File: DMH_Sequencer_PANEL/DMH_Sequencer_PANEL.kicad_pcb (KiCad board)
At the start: 2 copper layers, 100 x 200 mm, 5 parts, among them J0 Panel_GND_Solder_Wire_Pad

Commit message: Main controls position test ongoing
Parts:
- added H1: LED Step 1, SynthStuff:MountingHole_LED_3mm_R, F.Cu at (124.0, 46.5)
- added H10: CV 2, SynthStuff:Pot_Cutout_Small, F.Cu at (154.0, 65.0)
- added H1003: MountingHole_Rails, SynthStuff:MountingHole_Rails, F.Cu at (250.0, 33.5)
- added H1004: MountingHole_Rails, SynthStuff:MountingHole_Rails, F.Cu at (346.5, 33.5)
- added H1007: MountingHole_Rails, SynthStuff:MountingHole_Rails, F.Cu at (250.0, 226.5)
- added H1008: MountingHole_Rails, SynthStuff:MountingHole_Rails, F.Cu at (346.5, 226.5)
- added H11: CV 3, SynthStuff:Pot_Cutout_Small, F.Cu at (184.0, 65.0)
- added H12: CV 4, SynthStuff:Pot_Cutout_Small, F.Cu at (214.0, 65.0)
- added H13: CV 5, SynthStuff:Pot_Cutout_Small, F.Cu at (244.0, 65.0)
- added H14: CV 6, SynthStuff:Pot_Cutout_Small, F.Cu at (274.0, 65.0)
- added H15: CV 7, SynthStuff:Pot_Cutout_Small, F.Cu at (304.0, 65.0)
- added H16: CV 8, SynthStuff:Pot_Cutout_Small, F.Cu at (334.0, 65.0)
- added H17: GL 1, SynthStuff:Pot_Cutout_Tiny_gate_P110KH1, F.Cu at (124.0, 94.5)
- added H18: GL 2, SynthStuff:Pot_Cutout_Tiny_gate_P110KH1, F.Cu at (154.0, 94.5)
- added H19: GL 3, SynthStuff:Pot_Cutout_Tiny_gate_P110KH1, F.Cu at (184.0, 94.5)
- added H2: LED Step 2, SynthStuff:MountingHole_LED_3mm_R, F.Cu at (154.0, 46.5)
- added H20: GL 4, SynthStuff:Pot_Cutout_Tiny_gate_P110KH1, F.Cu at (214.0, 94.5)
- added H21: GL 5, SynthStuff:Pot_Cutout_Tiny_gate_P110KH1, F.Cu at (244.0, 94.5)
- added H22: GL 6, SynthStuff:Pot_Cutout_Tiny_gate_P110KH1, F.Cu at (274.0, 94.5)
- added H23: GL 7, SynthStuff:Pot_Cutout_Tiny_gate_P110KH1, F.Cu at (304.0, 94.5)
- added H24: GL 8, SynthStuff:Pot_Cutout_Tiny_gate_P110KH1, F.Cu at (334.0, 94.5)
- added H25: Slew 1, SynthStuff:Toggle_Switch_TE_Cutout, F.Cu at (598.6, 10.5)
- added H26: Slew 2, SynthStuff:Toggle_Switch_TE_Cutout, F.Cu at (613.7, 10.5)
- added H27: Slew 3, SynthStuff:Toggle_Switch_TE_Cutout, F.Cu at (628.7, 10.5)
- added H28: Slew 4, SynthStuff:Toggle_Switch_TE_Cutout, F.Cu at (643.7, 10.5)
- added H29: Slew 5, SynthStuff:Toggle_Switch_TE_Cutout, F.Cu at (598.6, 26.4)
- added H3: LED Step 3, SynthStuff:MountingHole_LED_3mm_R, F.Cu at (184.0, 46.5)
- added H30: Slew 6, SynthStuff:Toggle_Switch_TE_Cutout, F.Cu at (613.7, 26.4)
- added H31: Slew 7, SynthStuff:Toggle_Switch_TE_Cutout, F.Cu at (628.7, 26.4)
- added H32: Slew 8, SynthStuff:Toggle_Switch_TE_Cutout, F.Cu at (643.7, 26.4)
- added H33: LED Step 9, SynthStuff:MountingHole_LED_3mm_R, F.Cu at (605.0, 68.6)
- added H34: LED Step 10, SynthStuff:MountingHole_LED_3mm_R, F.Cu at (605.0, 74.1)
- added H35: LED Step 11, SynthStuff:MountingHole_LED_3mm_R, F.Cu at (605.0, 79.7)
- added H36: LED Step 12, SynthStuff:MountingHole_LED_3mm_R, F.Cu at (605.0, 85.2)
- added H37: LED Step 13, SynthStuff:MountingHole_LED_3mm_R, F.Cu at (610.6, 68.6)
- added H38: LED Step 14, SynthStuff:MountingHole_LED_3mm_R, F.Cu at (610.6, 74.1)
- added H39: LED Step 15, SynthStuff:MountingHole_LED_3mm_R, F.Cu at (610.6, 79.7)
- added H4: LED Step 4, SynthStuff:MountingHole_LED_3mm_R, F.Cu at (214.0, 46.5)
- added H40: LED Step 16, SynthStuff:MountingHole_LED_3mm_R, F.Cu at (610.6, 85.2)
- added H41: CV 9, SynthStuff:Pot_Cutout_Small, F.Cu at (543.9, 17.8)
- added H42: CV 10, SynthStuff:Pot_Cutout_Small, F.Cu at (543.9, 47.3)
- added H43: CV 11, SynthStuff:Pot_Cutout_Small, F.Cu at (543.9, 76.8)
- added H44: CV 12, SynthStuff:Pot_Cutout_Small, F.Cu at (543.9, 106.3)
- added H45: CV 13, SynthStuff:Pot_Cutout_Small, F.Cu at (575.4, 17.8)
- added H46: CV 14, SynthStuff:Pot_Cutout_Small, F.Cu at (575.4, 47.3)
- added H47: CV 15, SynthStuff:Pot_Cutout_Small, F.Cu at (575.4, 76.8)
- added H48: CV 16, SynthStuff:Pot_Cutout_Small, F.Cu at (575.4, 106.3)
- added H49: GL 9, SynthStuff:Pot_Cutout_Tiny_gate_P110KH1, F.Cu at (528.9, 132.8)
- added H5: LED Step 5, SynthStuff:MountingHole_LED_3mm_R, F.Cu at (244.0, 46.5)
- added H50: GL 10, SynthStuff:Pot_Cutout_Tiny_gate_P110KH1, F.Cu at (528.9, 157.1)
- added H51: GL 11, SynthStuff:Pot_Cutout_Tiny_gate_P110KH1, F.Cu at (528.9, 181.3)
- added H52: GL 12, SynthStuff:Pot_Cutout_Tiny_gate_P110KH1, F.Cu at (528.9, 205.6)
- added H53: GL 13, SynthStuff:Pot_Cutout_Tiny_gate_P110KH1, F.Cu at (554.4, 132.8)
- added H54: GL 14, SynthStuff:Pot_Cutout_Tiny_gate_P110KH1, F.Cu at (554.4, 157.1)
- added H55: GL 15, SynthStuff:Pot_Cutout_Tiny_gate_P110KH1, F.Cu at (554.4, 181.3)
- added H56: GL 16, SynthStuff:Pot_Cutout_Tiny_gate_P110KH1, F.Cu at (554.4, 205.6)
- added H57: Slew 9, SynthStuff:Toggle_Switch_TE_Cutout, F.Cu at (598.6, 42.4)
- added H58: Slew 10, SynthStuff:Toggle_Switch_TE_Cutout, F.Cu at (613.7, 42.4)
- added H59: Slew 11, SynthStuff:Toggle_Switch_TE_Cutout, F.Cu at (628.7, 42.4)
- added H6: LED Step 6, SynthStuff:MountingHole_LED_3mm_R, F.Cu at (274.0, 46.5)
- added H60: Slew 12, SynthStuff:Toggle_Switch_TE_Cutout, F.Cu at (643.7, 42.4)
- added H61: Slew 13, SynthStuff:Toggle_Switch_TE_Cutout, F.Cu at (598.6, 58.3)
- added H62: Slew 14, SynthStuff:Toggle_Switch_TE_Cutout, F.Cu at (613.7, 58.3)
- added H63: Slew 15, SynthStuff:Toggle_Switch_TE_Cutout, F.Cu at (628.7, 58.3)
- added H64: Slew 16, SynthStuff:Toggle_Switch_TE_Cutout, F.Cu at (643.7, 58.3)
- added H65: Gate Out 1, SynthStuff:Jack_6.35mm_Cutout_Output_v6, F.Cu at (575.7, 128.6)
- added H66: Gate Out 2, SynthStuff:Jack_6.35mm_Cutout_Output_v6, F.Cu at (575.7, 145.7)
- added H67: Gate Out 3, SynthStuff:Jack_6.35mm_Cutout_Output_v6, F.Cu at (592.8, 128.6)
- added H68: Gate Out 4, SynthStuff:Jack_6.35mm_Cutout_Output_v6, F.Cu at (592.8, 145.7)
- added H69: Gate Out 5, SynthStuff:Jack_6.35mm_Cutout_Output_v6, F.Cu at (609.9, 128.6)
- added H7: LED Step 7, SynthStuff:MountingHole_LED_3mm_R, F.Cu at (304.0, 46.5)
- added H70: Gate Out 6, SynthStuff:Jack_6.35mm_Cutout_Output_v6, F.Cu at (609.9, 145.7)
- added H71: Gate Out 7, SynthStuff:Jack_6.35mm_Cutout_Output_v6, F.Cu at (627.0, 128.6)
- added H72: Gate Out 8, SynthStuff:Jack_6.35mm_Cutout_Output_v6, F.Cu at (627.0, 145.7)
- added H8: LED Step 8, SynthStuff:MountingHole_LED_3mm_R, F.Cu at (334.0, 46.5)
- added H9: CV 1, SynthStuff:Pot_Cutout_Small, F.Cu at (124.0, 65.0)
- moved H1002 3.50 mm to (150.0, 33.5)
- moved H1006 3.50 mm to (150.0, 226.5)
- renumbered H1 to H1001, H2 to H1002, H3 to H1005, H4 to H1006
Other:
- board size 100 x 200 mm -> 300 x 200 mm
- board text added: "Sequencer"
- board text removed: "Name"

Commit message: First Layout ready
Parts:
- removed H65: Gate Out 1, SynthStuff:Jack_6.35mm_Cutout_Output_v6
- removed H66: Gate Out 2, SynthStuff:Jack_6.35mm_Cutout_Output_v6
- removed H67: Gate Out 3, SynthStuff:Jack_6.35mm_Cutout_Output_v6
- removed H68: Gate Out 4, SynthStuff:Jack_6.35mm_Cutout_Output_v6
- removed H69: Gate Out 5, SynthStuff:Jack_6.35mm_Cutout_Output_v6
- removed H70: Gate Out 6, SynthStuff:Jack_6.35mm_Cutout_Output_v6
- removed H71: Gate Out 7, SynthStuff:Jack_6.35mm_Cutout_Output_v6
- removed H72: Gate Out 8, SynthStuff:Jack_6.35mm_Cutout_Output_v6
- added H73: Clock, SynthStuff:Pot_Cutout_Medium_v2, F.Cu at (80.5, 55.0)
- added H75: Transp, SynthStuff:Pot_Cutout_Tiny, F.Cu at (94.5, 87.0)
- added H77: Slew, SynthStuff:Pot_Cutout_Tiny, F.Cu at (66.5, 87.0)
- added H79: Direction, SynthStuff:Selector_Cutout_5pos, F.Cu at (80.5, 121.5)
- added H80: Mode, SynthStuff:Toggle_Switch_TE_Cutout, F.Cu at (95.0, 171.0)
- added H81: Clock, SynthStuff:Toggle_Switch_TE_Cutout, F.Cu at (66.0, 171.0)
- added H82: Quant, SynthStuff:Toggle_Switch_TE_Cutout, F.Cu at (80.5, 171.0)
- added H83: Step, SynthStuff:MX_switch_Cutout, F.Cu at (66.0, 148.0)
- added H84: Reset, SynthStuff:MX_switch_Cutout, F.Cu at (95.0, 148.0)
- added H85: LED Quant, SynthStuff:MountingHole_LED_3mm_R, F.Cu at (80.5, 148.0)
- added H86: CV 1-8, SynthStuff:Jack_6.35mm_Cutout_Output_v6, F.Cu at (63.4, 208.8)
- added H87: CV 9-16, SynthStuff:Jack_6.35mm_Cutout_Output_v6, F.Cu at (80.5, 208.8)
- added H88: Gate, SynthStuff:Jack_6.35mm_Cutout_Output_v6, F.Cu at (97.6, 208.8)
- added H90: Clock, SynthStuff:Jack_6.35mm_Cutout_v3, F.Cu at (63.4, 190.2)
- added H91: Reset, SynthStuff:Jack_6.35mm_Cutout_v3, F.Cu at (80.5, 190.2)
- added H92: Transp, SynthStuff:Jack_6.35mm_Cutout_v3, F.Cu at (97.6, 190.2)
- moved H57 502.9 mm to (124.0, 208.5)
- moved H58 488.8 mm to (154.0, 208.5)
- moved H25 486.7 mm to (124.0, 118.0)
- moved H33 485.6 mm to (124.0, 135.5)
- moved H59 474.7 mm to (184.0, 208.5)
- moved H26 472.1 mm to (154.0, 118.0)
- moved H60 460.7 mm to (214.0, 208.5)
- moved H27 457.5 mm to (184.0, 118.0)
- moved H34 455.2 mm to (154.0, 135.5)
- moved H28 442.9 mm to (214.0, 118.0)
- moved H41 441.4 mm to (124.0, 154.0)
- moved H35 424.7 mm to (184.0, 135.5)
- moved H49 408.2 mm to (124.0, 185.0)
- moved H42 404.2 mm to (154.0, 154.0)
- moved H36 394.2 mm to (214.0, 135.5)
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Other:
- board text added: "1x16"
- board text added: "2x8"
- board text added: "Dis"
- board text added: "En"

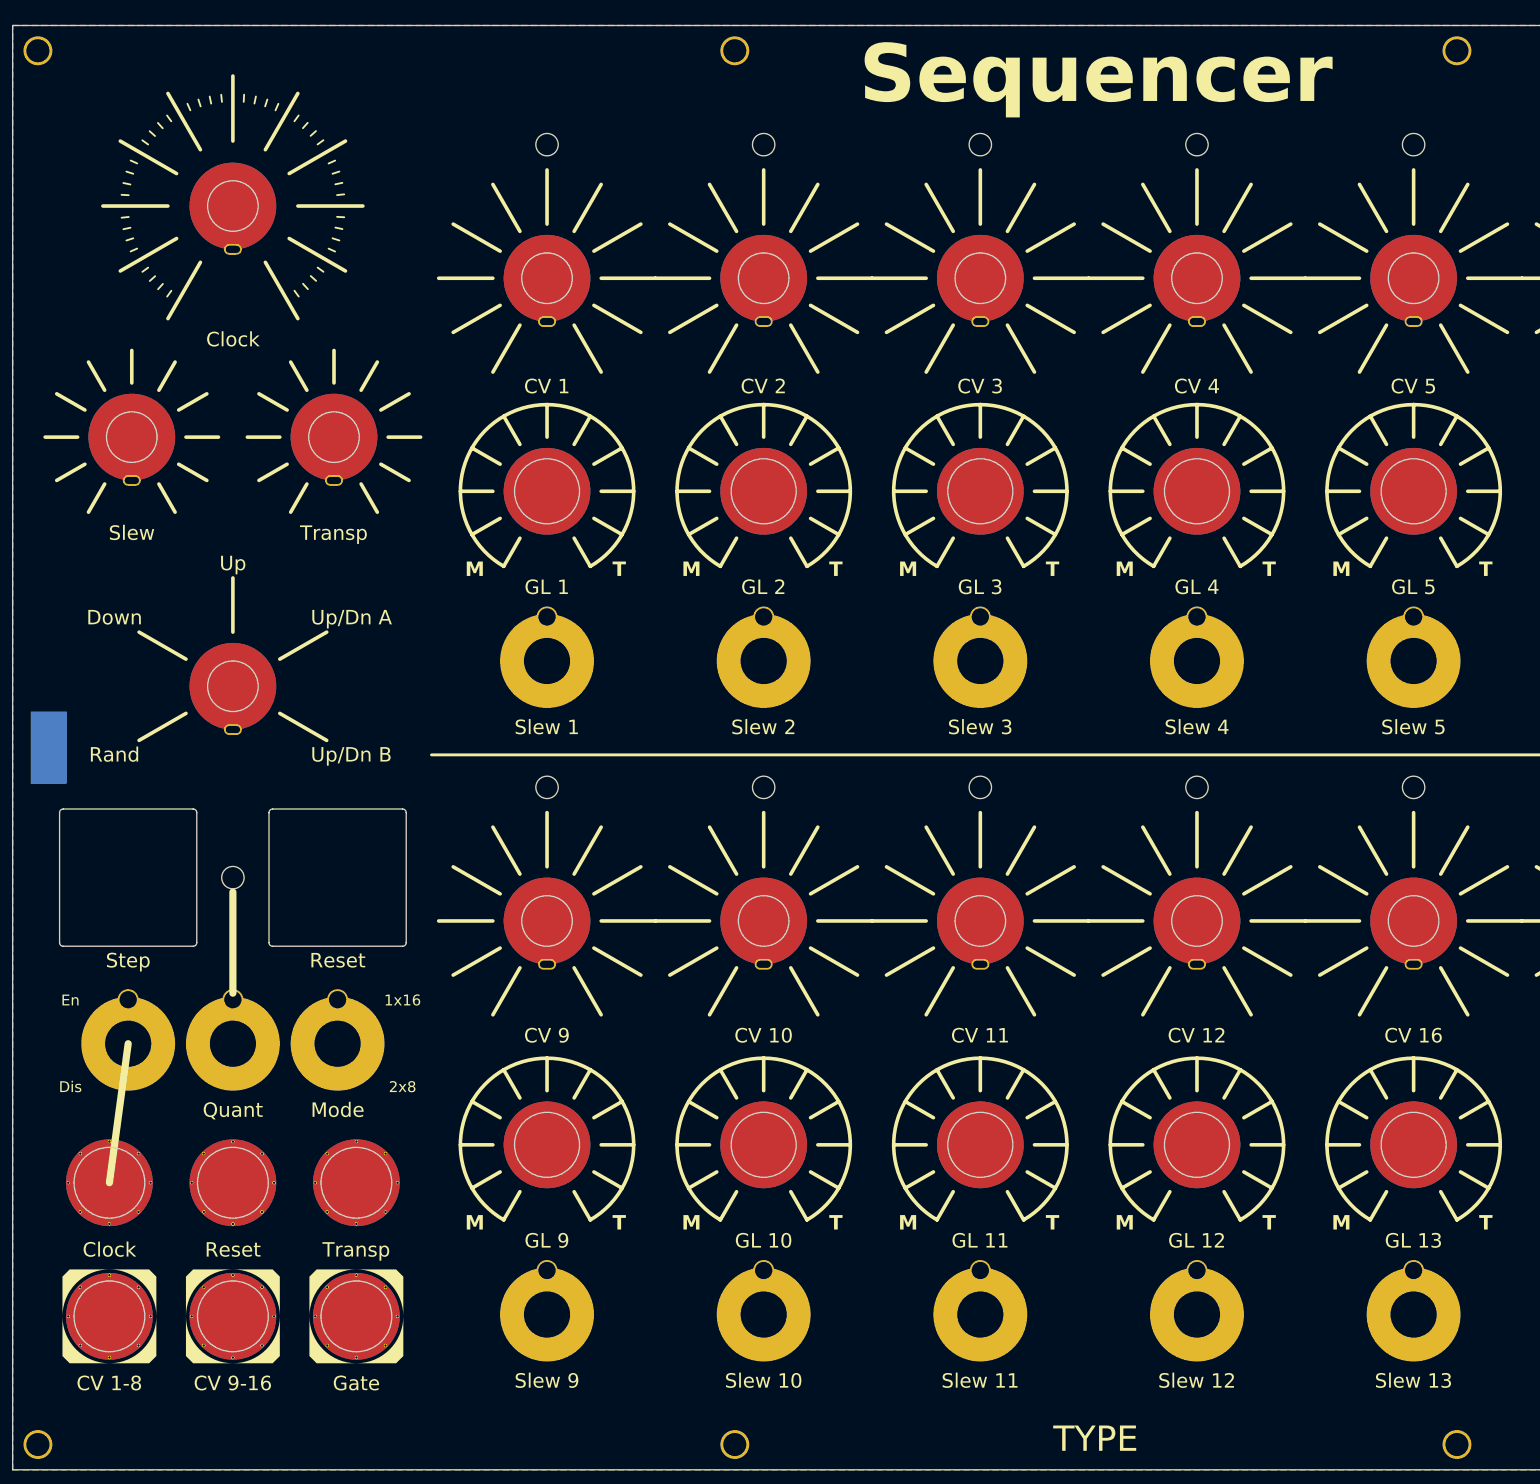
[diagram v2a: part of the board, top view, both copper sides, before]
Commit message: Updated selector 3D model
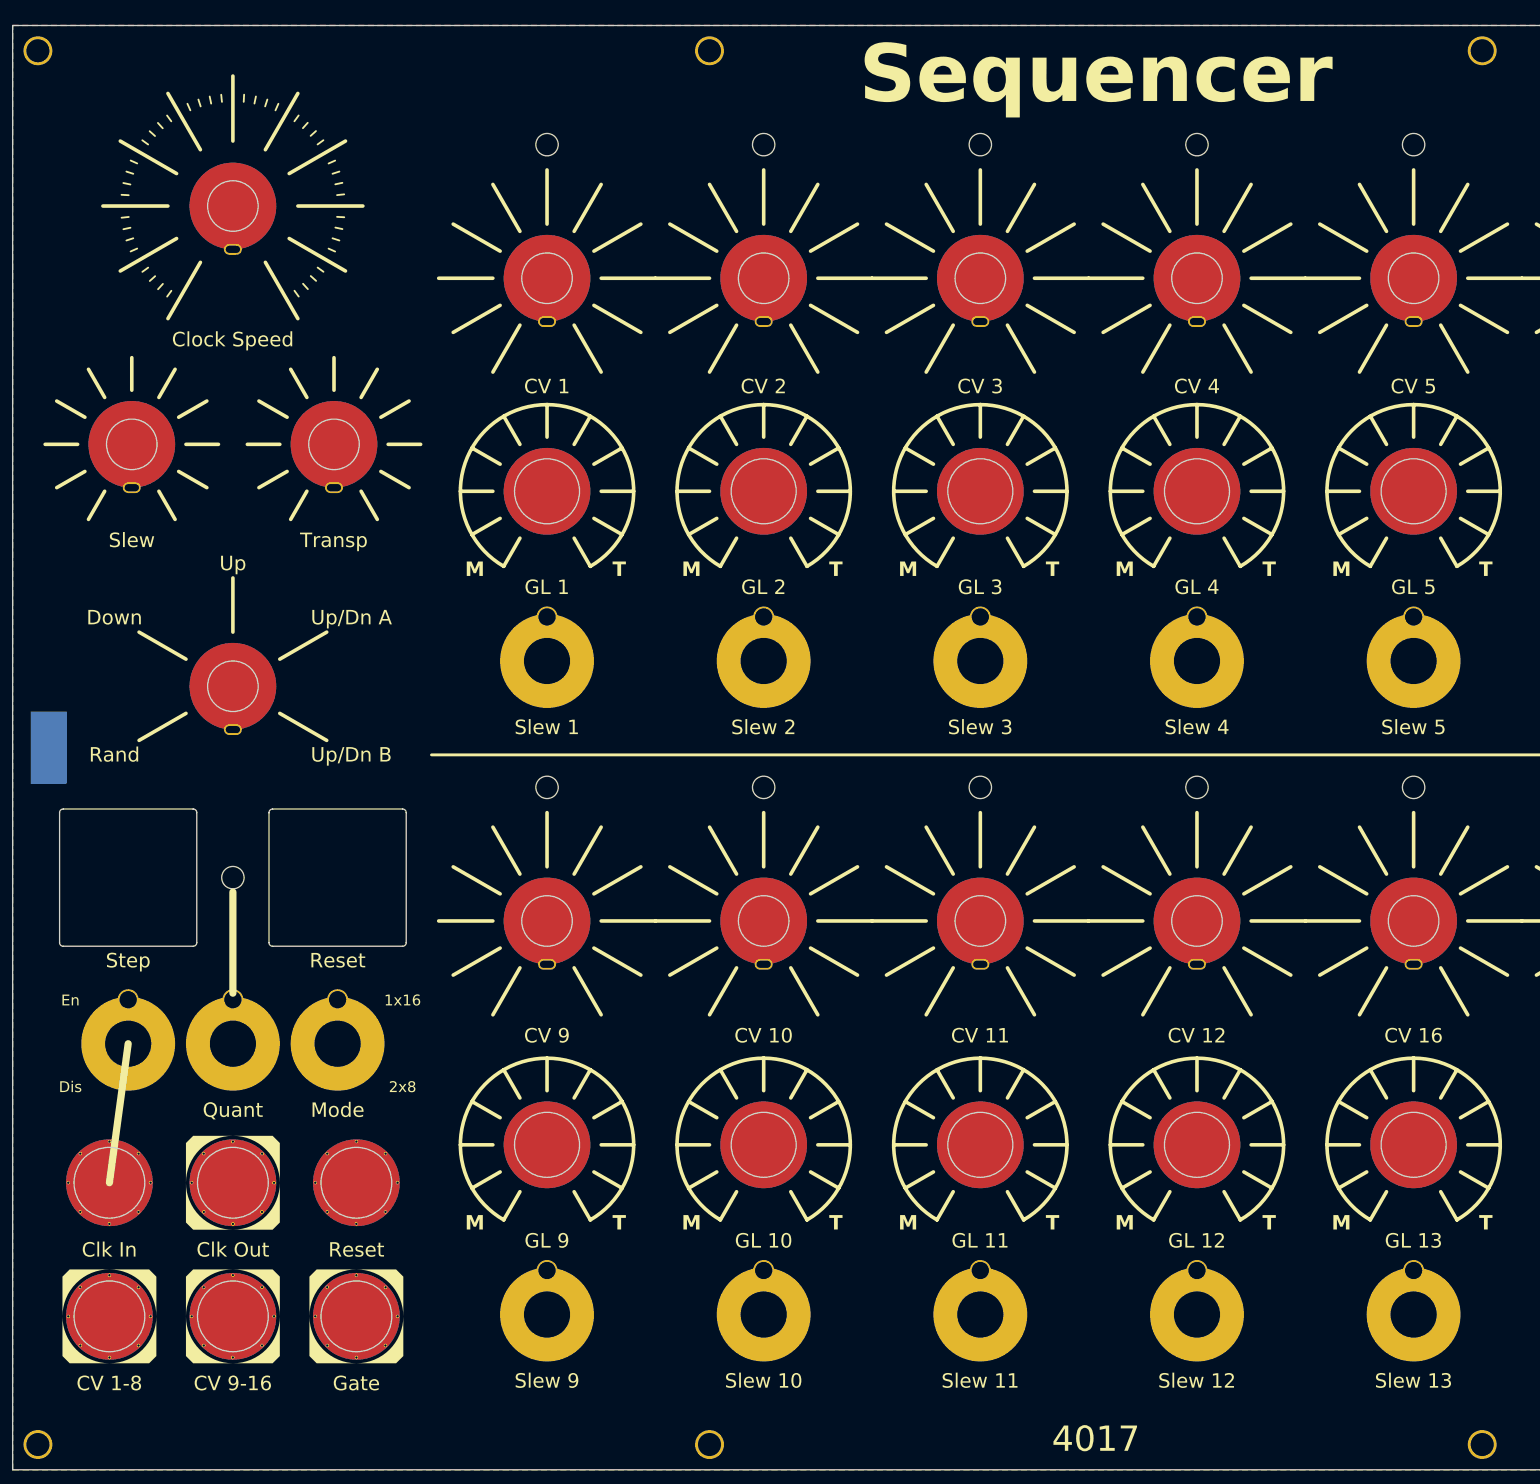
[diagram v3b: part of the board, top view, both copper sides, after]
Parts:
- removed H92: Transp, SynthStuff:Jack_6.35mm_Cutout_v3
- added H97: Clk Out, SynthStuff:Jack_6.35mm_Cutout_Output_v6, F.Cu at (80.5, 190.2)
- H73: value Clock -> Clock Speed
- H85: footprint SynthStuff:MountingHole_LED_3mm_R -> SynthStuff:MountingHole_LED_3mm_B
- H90: value Clock -> Clk In
- moved H91 17.1 mm to (97.6, 190.2)
- moved H1002 3.50 mm to (146.5, 33.5)
- moved H1003 3.50 mm to (253.5, 33.5)
- moved H1006 3.50 mm to (146.5, 226.5)
- moved H1007 3.50 mm to (253.5, 226.5)
- moved H75 1.00 mm to (94.5, 88.0)
- moved H77 1.00 mm to (66.5, 88.0)
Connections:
- H10 pad 1: unconnected-(H10-Pad1) -> GND
- H11 pad 1: unconnected-(H11-Pad1) -> GND
- H12 pad 1: unconnected-(H12-Pad1) -> GND
- H13 pad 1: unconnected-(H13-Pad1) -> GND
- H14 pad 1: unconnected-(H14-Pad1) -> GND
- H15 pad 1: unconnected-(H15-Pad1) -> GND
- H16 pad 1: unconnected-(H16-Pad1) -> GND
- H17 pad 1: unconnected-(H17-Pad1) -> GND
- H18 pad 1: unconnected-(H18-Pad1) -> GND
- H19 pad 1: unconnected-(H19-Pad1) -> GND
- H20 pad 1: unconnected-(H20-Pad1) -> GND
- H21 pad 1: unconnected-(H21-Pad1) -> GND
- H22 pad 1: unconnected-(H22-Pad1) -> GND
- H23 pad 1: unconnected-(H23-Pad1) -> GND
- H24 pad 1: unconnected-(H24-Pad1) -> GND
- H25 pad 1: unconnected-(H25-Pad1) -> GND
- H26 pad 1: unconnected-(H26-Pad1) -> GND
- H27 pad 1: unconnected-(H27-Pad1) -> GND
- H28 pad 1: unconnected-(H28-Pad1) -> GND
- H29 pad 1: unconnected-(H29-Pad1) -> GND
- H30 pad 1: unconnected-(H30-Pad1) -> GND
- H31 pad 1: unconnected-(H31-Pad1) -> GND
- H32 pad 1: unconnected-(H32-Pad1) -> GND
- H41 pad 1: unconnected-(H41-Pad1) -> GND
- H42 pad 1: unconnected-(H42-Pad1) -> GND
- H43 pad 1: unconnected-(H43-Pad1) -> GND
- H44 pad 1: unconnected-(H44-Pad1) -> GND
- H45 pad 1: unconnected-(H45-Pad1) -> GND
- H46 pad 1: unconnected-(H46-Pad1) -> GND
- H47 pad 1: unconnected-(H47-Pad1) -> GND
- H48 pad 1: unconnected-(H48-Pad1) -> GND
- H49 pad 1: unconnected-(H49-Pad1) -> GND
- H50 pad 1: unconnected-(H50-Pad1) -> GND
- H51 pad 1: unconnected-(H51-Pad1) -> GND
- H52 pad 1: unconnected-(H52-Pad1) -> GND
- H53 pad 1: unconnected-(H53-Pad1) -> GND
- H54 pad 1: unconnected-(H54-Pad1) -> GND
- H55 pad 1: unconnected-(H55-Pad1) -> GND
- H56 pad 1: unconnected-(H56-Pad1) -> GND
- H57 pad 1: unconnected-(H57-Pad1) -> GND
- H58 pad 1: unconnected-(H58-Pad1) -> GND
- H59 pad 1: unconnected-(H59-Pad1) -> GND
- H60 pad 1: unconnected-(H60-Pad1) -> GND
- H61 pad 1: unconnected-(H61-Pad1) -> GND
- H62 pad 1: unconnected-(H62-Pad1) -> GND
- H63 pad 1: unconnected-(H63-Pad1) -> GND
- H64 pad 1: unconnected-(H64-Pad1) -> GND
- H73 pad 1: unconnected-(H73-Pad1) -> GND
- H75 pad 1: unconnected-(H75-Pad1) -> GND
- H77 pad 1: unconnected-(H77-Pad1) -> GND
- H79 pad 1: unconnected-(H79-Pad1) -> GND
- H80 pad 1: unconnected-(H80-Pad1) -> GND
- H81 pad 1: unconnected-(H81-Pad1) -> GND
- H82 pad 1: unconnected-(H82-Pad1) -> GND
- H86 pad 1: unconnected-(H86-Pad1) -> GND
- H87 pad 1: unconnected-(H87-Pad1) -> GND
- H88 pad 1: unconnected-(H88-Pad1) -> GND
- H9 pad 1: unconnected-(H9-Pad1) -> GND
- H90 pad 1: unconnected-(H90-Pad1) -> GND
- H91 pad 1: unconnected-(H91-Pad1) -> GND
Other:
- board text added: "4017"
- board text removed: "TYPE"
